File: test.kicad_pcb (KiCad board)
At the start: 4 copper layers, 112.7 x 43 mm, 85 parts, among them IC1 LC709203FQH-01TWG, IC2 BQ24074RGTR, IC3 USBLC6-2SC6, IC4 ESP32-S3-WROOM-1-N16, IC5 MCP6S91-E_MS, IC6 MCP6S91-E_MS, IC7 MCP4726A1T-E_CH, IC8 MCP4726A1T-E_CH, J1 UART0, J2 73100-0105, J3 73100-0105, K1 AQY210EHA, K2 AQY210EHA, SW1 Reset, SW2 Boot, U1 1043, U1 USB-C_SMD-TYPE-C-31-M-12, U2 1043, U4 LD1086DT33TR, U5 LD1086DT33TR, U6 LD1086DT33TR, U7 ADC08351CILQX/NOPB, U8 ADC08351CILQX/NOPB

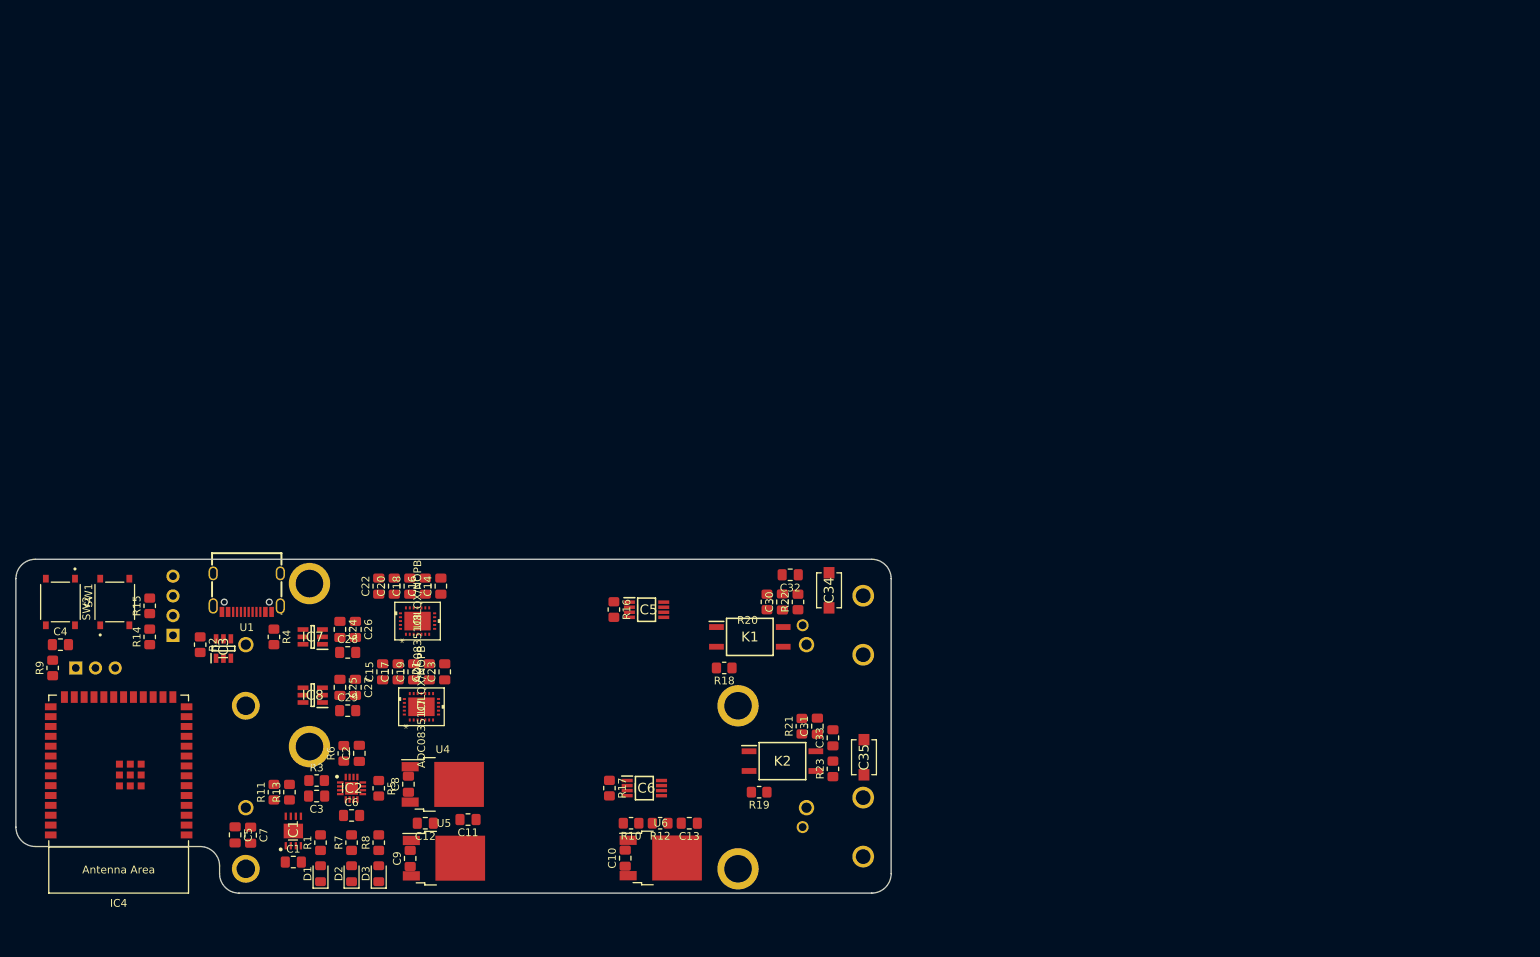
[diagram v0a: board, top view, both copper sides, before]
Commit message: layout for changed chematic
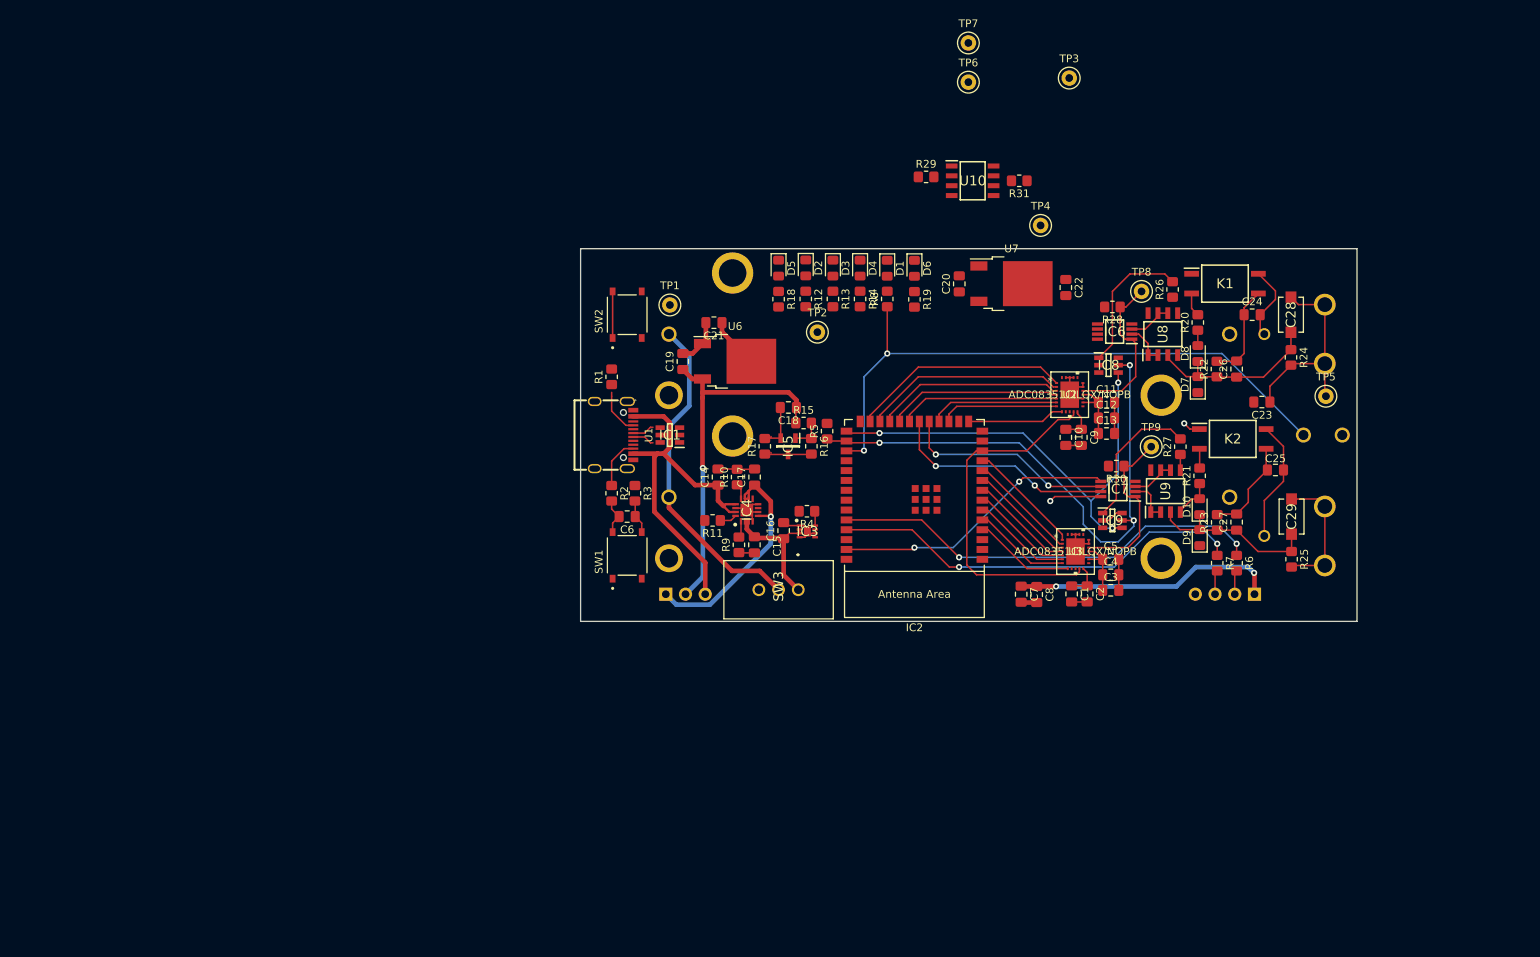
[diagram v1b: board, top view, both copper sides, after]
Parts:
- removed the C1 at (63.0, 129.0)
- removed the C10 at (105.8, 128.5)
- removed the C11 at (85.5, 123.5)
- removed the C12 at (80.0, 124.0)
- removed the C13 at (114.0, 124.0)
- removed the C2 at (71.5, 115.0)
- removed the C3 at (66.0, 120.5)
- removed C30, C31: 47n, Capacitor_SMD:C_0805_2012Metric_Pad1.18x1.45mm_HandSolder
- removed C32, C33: 100n, Capacitor_SMD:C_0805_2012Metric_Pad1.18x1.45mm_HandSolder
- removed C34, C35: 5.5p-30p var, project_library:JZ300
- removed the C6 at (70.5, 123.0)
- removed the C8 at (77.8, 119.0)
- removed the C9 at (78.0, 128.5)
- removed the IC1 at (63.0, 125.0)
- removed the IC2 at (70.5, 119.5)
- removed the J2 at (154.0, 124.5)
- removed the R2 at (51.0, 101.0)
- removed the R3 at (66.0, 118.5)
- removed the R6 at (69.5, 115.0)
- removed the R7 at (70.5, 126.5)
- removed the U1 at (56.9, 101.0)
- removed the U2 at (56.9, 122.0)
- added C14: 1u, Capacitor_SMD:C_0805_2012Metric_Pad1.18x1.45mm_HandSolder, F.Cu at (117.7, 79.4)
- added C15: 4u7, Capacitor_SMD:C_0805_2012Metric_Pad1.18x1.45mm_HandSolder, F.Cu at (122.4, 88.1)
- added C16: 0.1u, Capacitor_SMD:C_0805_2012Metric_Pad1.18x1.45mm_HandSolder, F.Cu at (126.2, 86.3)
- added C17: 4u7, Capacitor_SMD:C_0805_2012Metric_Pad1.18x1.45mm_HandSolder, F.Cu at (122.4, 79.4)
- added C18: 1u, Capacitor_SMD:C_0805_2012Metric_Pad1.18x1.45mm_HandSolder, F.Cu at (126.8, 70.5)
- added C19: 10u, Capacitor_SMD:C_0805_2012Metric_Pad1.18x1.45mm_HandSolder, F.Cu at (113.2, 64.5)
- added C20: 10u, Capacitor_SMD:C_0805_2012Metric_Pad1.18x1.45mm_HandSolder, F.Cu at (148.8, 54.5)
- added C21: 10u, Capacitor_SMD:C_0805_2012Metric_Pad1.18x1.45mm_HandSolder, F.Cu at (117.2, 59.5)
- added C22: 10u, Capacitor_SMD:C_0805_2012Metric_Pad1.18x1.45mm_HandSolder, F.Cu at (162.5, 55.0)
- added C23: 1u, Capacitor_SMD:C_0805_2012Metric_Pad1.18x1.45mm_HandSolder, F.Cu at (187.8, 69.8)
- added D10: ~, Diode_SMD:D_0805_2012Metric_Pad1.15x1.40mm_HandSolder, F.Cu at (179.7, 83.2)
- added D4: LOW_BATTERY, LED_SMD:LED_0805_2012Metric_Pad1.15x1.40mm_HandSolder, F.Cu at (136.0, 52.5)
- added D5: 3.3V, LED_SMD:LED_0805_2012Metric_Pad1.15x1.40mm_HandSolder, F.Cu at (125.5, 52.5)
- added D6: 3.3VA, LED_SMD:LED_0805_2012Metric_Pad1.15x1.40mm_HandSolder, F.Cu at (143.0, 52.5)
- added D7: ~, Diode_SMD:D_0805_2012Metric_Pad1.15x1.40mm_HandSolder, F.Cu at (179.5, 67.5)
- added D8: ~, Diode_SMD:D_0805_2012Metric_Pad1.15x1.40mm_HandSolder, F.Cu at (179.5, 63.5)
- added D9: ~, Diode_SMD:D_0805_2012Metric_Pad1.15x1.40mm_HandSolder, F.Cu at (179.8, 87.2)
- added IC3: MAX17048G+T10, project_library:MAX17048G+T10, F.Cu at (129.2, 86.4)
- added IC4: BQ24074RGTR, project_library:BQ24074RGTR, F.Cu at (121.4, 83.7)
- added IC9: DAC5571IDBVR, project_library:DAC5571IDBVR, F.Cu at (168.5, 85.0)
- added J1: PWM, project_library:725996-2, B.Cu at (199.0, 74.0)
- added J4: ~, project_library:73100-0105, B.Cu at (213.5, 87.0)
- added R14: 1k5, Resistor_SMD:R_0805_2012Metric_Pad1.20x1.40mm_HandSolder, F.Cu at (136.0, 56.5)
- added R15: 3k3, Resistor_SMD:R_0805_2012Metric_Pad1.20x1.40mm_HandSolder, F.Cu at (128.7, 72.5)
- added R24: ~, Resistor_SMD:R_0805_2012Metric_Pad1.20x1.40mm_HandSolder, F.Cu at (191.5, 64.0)
- added R25: ~, Resistor_SMD:R_0805_2012Metric_Pad1.20x1.40mm_HandSolder, F.Cu at (191.6, 90.0)
- added R26: ~, Resistor_SMD:R_0805_2012Metric_Pad1.20x1.40mm_HandSolder, F.Cu at (176.2, 55.2)
- added R27: ~, Resistor_SMD:R_0805_2012Metric_Pad1.20x1.40mm_HandSolder, F.Cu at (177.2, 75.5)
- added R28: ~, Resistor_SMD:R_0805_2012Metric_Pad1.20x1.40mm_HandSolder, F.Cu at (168.5, 57.5)
- added R29: ~, Resistor_SMD:R_0805_2012Metric_Pad1.20x1.40mm_HandSolder, F.Cu at (144.5, 40.8)
- added R30: ~, Resistor_SMD:R_0805_2012Metric_Pad1.20x1.40mm_HandSolder, F.Cu at (169.0, 78.0)
- added R31: ~, Resistor_SMD:R_0805_2012Metric_Pad1.20x1.40mm_HandSolder, F.Cu at (156.5, 41.2)
- added R4: 5k, Resistor_SMD:R_0805_2012Metric_Pad1.20x1.40mm_HandSolder, F.Cu at (129.2, 83.8)
- added R9: 10k, Resistor_SMD:R_0805_2012Metric_Pad1.20x1.40mm_HandSolder, F.Cu at (120.4, 88.1)
- added SW3: SW_DPDT_x2, project_library:25136NAH6, F.Cu at (125.5, 93.5)
- added TP1: VBat, TestPoint:TestPoint_Keystone_5000-5004_Miniature, F.Cu at (111.5, 57.2)
- added TP2: VBatChargeIC, TestPoint:TestPoint_Keystone_5000-5004_Miniature, F.Cu at (130.5, 60.8)
- added TP3: 3.3V, TestPoint:TestPoint_Keystone_5000-5004_Miniature, F.Cu at (162.9, 28.0)
- added TP4: 3.3VA, TestPoint:TestPoint_Keystone_5000-5004_Miniature, F.Cu at (159.2, 47.0)
- added TP5: GNDREF, TestPoint:TestPoint_Keystone_5000-5004_Miniature, F.Cu at (196.0, 69.0)
- added TP6: ~, TestPoint:TestPoint_Keystone_5000-5004_Miniature, F.Cu at (149.9, 28.6)
- added TP7: ~, TestPoint:TestPoint_Keystone_5000-5004_Miniature, F.Cu at (149.9, 23.5)
- added TP8: ~, TestPoint:TestPoint_Keystone_5000-5004_Miniature, F.Cu at (172.2, 55.5)
- added TP9: ~, TestPoint:TestPoint_Keystone_5000-5004_Miniature, F.Cu at (173.5, 75.5)
- added U10: ~, project_library:MCP6022T-I_SN, F.Cu at (150.5, 41.2)
- added U7: LD1086DT33TR, Package_TO_SOT_SMD:TO-252-2, F.Cu at (155.5, 54.5)
- added U8: ~, project_library:MCP6022T-I_SN, F.Cu at (175.0, 61.0)
- added U9: ~, project_library:MCP6022T-I_SN, F.Cu at (175.3, 81.2)
- C24, C25: value 0.1u -> ~
- C26, C27: value 10u -> ~
- C28, C29: value 0.1u -> ~; footprint Capacitor_SMD:C_0805_2012Metric_Pad1.18x1.45mm_HandSolder -> project_library:JZ300
- D1: value LOW_BATTERY -> Status
- IC5: value MCP6S91-E_MS -> LM4041CEM3-ADJ_NOPB; footprint project_library:MCP6S91-E_MS -> project_library:LM4041CEM3-ADJ_NOPB
- IC6: value MCP6S91-E_MS -> ~
- IC7: value MCP4726A1T-E_CH -> ~; footprint project_library:MCP4726A1T-E_CH -> project_library:MCP6S91-E_MS
- IC8: value MCP4726A1T-E_CH -> DAC5571IDBVR; footprint project_library:MCP4726A1T-E_CH -> project_library:DAC5571IDBVR
- J3: value 73100-0105 -> ~
- JP1: value Jumper_3_Open -> Power_Select
- K1, K2: value AQY210EHA -> ~
- R1: value 1k5 -> 5k1
- R10: value 39 -> 1k
- R11: value 5k -> 820
- R12: value 120 -> 1k5
- R13: value 5k -> 1k5
- R16: value 5k1 -> 1k
- R17: value 5k1 -> 330
- R18, R19: value 1k -> 1k5
- R20, R21: value 100k -> ~
- R22, R23: value 910k -> ~
- R5: value 1k -> 5k
- SW2: value Boot -> Button
- U4, U5: value LD1086DT33TR -> 1043; footprint Package_TO_SOT_SMD:TO-252-2 -> project_library:1043; moved to B.Cu
- moved R6 140.3 mm to (184.5, 90.5), turned to -90 degrees
- moved J2 139.4 mm to (186.8, 94.5), turned to 90 degrees
- moved R7 137.6 mm to (182.0, 90.5), turned to -90 degrees
- moved C28 129.1 mm to (191.5, 58.5), turned to 90 degrees
- moved C24 124.3 mm to (186.5, 58.5), turned to 0 degrees
- moved C29 124.1 mm to (191.6, 84.5), turned to 90 degrees
- moved C25 123.7 mm to (189.5, 78.5), turned to 0 degrees
- moved C26 118.4 mm to (184.5, 65.5), turned to 90 degrees
- moved C27 115.5 mm to (184.5, 85.2), turned to 90 degrees
- moved IC8 111.0 mm to (168.0, 65.0), turned to 0 degrees
- moved IC2 108.5 mm to (143.0, 81.8)
- moved D1 106.8 mm to (139.5, 52.5), turned to -90 degrees
- moved C7 105.9 mm to (156.8, 94.5)
- moved C8 105.9 mm to (158.8, 94.5)
- moved IC7 105.4 mm to (169.2, 81.0)
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- renumbered C14 to C1, C17 to C10, C19 to C11, C21 to C12, C23 to C13, C16 to C2, C18 to C3, C20 to C4, C22 to C5, C4 to C6, C5 to C7, C7 to C8, C15 to C9, IC3 to IC1, IC4 to IC2, J1 to J2, R4 to R2, R9 to R3, R14 to R6, R15 to R7, U7 to U2, U8 to U3
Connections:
- net /Charging renamed Charging
- net Net-(IC3-Pad4) renamed /D+
- net Net-(IC3-Pad6) renamed /D-
- C24 pad 2: GND -> Net-(C24-Pad2)
- C25 pad 2: GND -> Net-(C25-Pad2)
- C26 pad 1: Net-(C24-Pad1) -> Net-(C26-Pad1)
- C26 pad 2: GND -> Net-(C24-Pad1)
- C27 pad 1: Net-(C25-Pad1) -> Net-(C27-Pad1)
- C27 pad 2: GND -> Net-(C25-Pad1)
- C28 pad 1: Net-(C28-Pad1) -> Net-(C26-Pad1)
- C28 pad 2: GND -> GNDREF
- C29 pad 1: Net-(C29-Pad1) -> Net-(C27-Pad1)
- C29 pad 2: GND -> GNDREF
- IC2 pad 10: /CH1_D1 -> /CH2_D1
- IC2 pad 11: /CH1_D0 -> /CH2_D0
- IC2 pad 15: /CH2_D7 -> /CH1_D7
- IC2 pad 16: /LOG -> unconnected-(IC2-Pad16)
- IC2 pad 17: /CH2_D6 -> /CH1_D6
- IC2 pad 18: /CH2_D5 -> /CH1_D5
- IC2 pad 19: /MOSI -> MOSI
- IC2 pad 20: /SCLK -> SCLK_SPI
- IC2 pad 21: /CH2_D4 -> /CH1_D4
- IC2 pad 22: /CH2_D3 -> /CH1_D3
- IC2 pad 23: /CH2_D2 -> /CH1_D2
- IC2 pad 24: /CH2_D1 -> /CH1_D1
- IC2 pad 25: /CH2_D0 -> /CH1_D0
- IC2 pad 26: /VSPI -> unconnected-(IC2-Pad26)
- IC2 pad 27: /BOOT -> SDA
- IC2 pad 28: unconnected-(IC4-Pad28) -> SCL_I2C
- IC2 pad 29: unconnected-(IC4-Pad29) -> /Status_PWM
- IC2 pad 30: unconnected-(IC4-Pad30) -> Trigger_Ref
- IC2 pad 31: /CH1_Gnd_Sel -> Trigger_CH1
- IC2 pad 32: /CH2_Gnd_Sel -> Trigger_CH2
- IC2 pad 33: /CS_A -> CH1_AC_Sel
- IC2 pad 34: /CS_B -> CH2_AC_Sel
- IC2 pad 38: /SCL -> CS_Gain_CH1
- IC2 pad 39: /SDA -> CS_Gain_CH2
- IC2 pad 4: /CH1_D7 -> /CH2_D7
- IC2 pad 5: /CH1_D6 -> /CH2_D6
- IC2 pad 6: /CH1_D5 -> /CH2_D5
- IC2 pad 7: /CH1_D4 -> /CH2_D4
- IC2 pad 8: /CH1_D3 -> /CH2_D3
- IC2 pad 9: /CH1_D2 -> /CH2_D2
- IC5 pad 1: Net-(IC5-Pad1) -> GNDREF
- IC5 pad 2: unconnected-(IC5-Pad2) -> GNDA
- IC5 pad 3: GND -> Net-(IC5-Pad3)
- IC6 pad 1: Net-(IC6-Pad1) -> Analog_Out_CH1
- IC6 pad 2: unconnected-(IC6-Pad2) -> Net-(IC6-Pad2)
- IC6 pad 3: GND -> Net-(IC6-Pad3)
- IC6 pad 5: /CS_A -> CS_Gain_CH1
- IC6 pad 6: /MOSI -> MOSI
- IC6 pad 7: /SCLK -> SCLK_SPI
- IC6 pad 8: +3V3 -> +3.3VA
- IC7 pad 1: Net-(C28-Pad1) -> Analog_Out_CH2
- IC7 pad 2: GND -> Net-(IC7-Pad2)
- IC7 pad 3: Net-(C24-Pad1) -> Net-(IC7-Pad3)
- IC7 pad 4: /SDA -> GND
- IC7 pad 5: /SCL -> CS_Gain_CH2
- IC7 pad 6: unconnected-(IC7-Pad6) -> MOSI
- IC8 pad 1: Net-(C29-Pad1) -> /Analog/Offset_CH1
- IC8 pad 3: Net-(C25-Pad1) -> +3.3VA
- IC8 pad 4: /SDA -> SDA
- IC8 pad 5: /SCL -> SCL_I2C
- IC8 pad 6: unconnected-(IC8-Pad6) -> +3V3
- J3 pad 1: GND -> GNDREF
- J3 pad 2: GND -> GNDREF
- J3 pad 3: Net-(C35-Pad1) -> Net-(C24-Pad2)
- JP1 pad 1: /Vbat -> Net-(C17-Pad1)
- JP1 pad 2: Net-(C10-Pad1) -> Net-(C18-Pad1)
- K1 pad 1: /CH1_Gnd_Sel -> CH1_AC_Sel
- K1 pad 3: Net-(C32-Pad1) -> Net-(C24-Pad1)
- K1 pad 4: Net-(C30-Pad1) -> Net-(C24-Pad2)
- K2 pad 1: /CH2_Gnd_Sel -> CH2_AC_Sel
- K2 pad 3: Net-(C33-Pad1) -> Net-(C25-Pad1)
- K2 pad 4: Net-(C31-Pad1) -> Net-(C25-Pad2)
- R1 pad 1: Net-(D1-Pad2) -> Net-(R1-Pad1)
- R1 pad 2: /Alarm -> GND
- R10 pad 1: Net-(R10-Pad1) -> Net-(IC4-Pad12)
- R11 pad 1: /SCL -> Net-(IC4-Pad16)
- R11 pad 2: +3V3 -> GND
- R12 pad 1: GND -> Net-(D2-Pad2)
- R12 pad 2: Net-(R10-Pad1) -> Net-(C17-Pad1)
- R13 pad 1: /SDA -> Net-(D3-Pad2)
- R13 pad 2: +3V3 -> Net-(C17-Pad1)
- R16 pad 1: Net-(IC5-Pad1) -> GNDREF
- R16 pad 2: GND -> Net-(IC5-Pad3)
- R17 pad 1: Net-(IC6-Pad1) -> Net-(IC5-Pad3)
- R17 pad 2: GND -> GNDA
- R18 pad 1: GND -> Net-(D5-Pad2)
- R18 pad 2: Net-(K1-Pad2) -> +3V3
- R19 pad 1: GND -> Net-(D6-Pad2)
- R19 pad 2: Net-(K2-Pad2) -> +3.3VA
- R2 pad 1: Net-(R4-Pad1) -> Net-(R2-Pad1)
- R20 pad 1: Net-(C30-Pad1) -> GNDA
- R20 pad 2: GND -> Net-(K1-Pad2)
- R21 pad 1: Net-(C31-Pad1) -> GNDA
- R21 pad 2: GND -> Net-(K2-Pad2)
- R22 pad 1: Net-(C34-Pad1) -> Net-(C26-Pad1)
- R22 pad 2: Net-(C32-Pad1) -> Net-(C24-Pad1)
- R23 pad 1: Net-(C35-Pad1) -> Net-(C27-Pad1)
- R23 pad 2: Net-(C33-Pad1) -> Net-(C25-Pad1)
- R5 pad 1: Net-(IC2-Pad12) -> SCL_I2C
- R5 pad 2: GND -> +3V3
- R8 pad 1: Net-(D3-Pad2) -> /Status_PWM
- R8 pad 2: /Vbat -> Net-(D1-Pad2)
- SW1 pad A: GND -> unconnected-(SW1-PadA)
- SW1 pad C: /ENABLE -> unconnected-(SW1-PadC)
- SW2 pad A: /BOOT -> SDA
- SW2 pad B: /BOOT -> SDA
- U2 pad 10: +3V3 -> unconnected-(U2-Pad10)
- U2 pad 14: unconnected-(U7-Pad14) -> +3.3VA
- U2 pad 17: unconnected-(U7-Pad17) -> Analog_Out_CH1
- U2 pad 25: (no net) -> GND
- U3 pad 10: +3V3 -> unconnected-(U3-Pad10)
- U3 pad 17: unconnected-(U8-Pad17) -> Analog_Out_CH2
- U3 pad 25: (no net) -> GND
- U4 pad 1: GND -> /Power Supply/VBat+
- U4 pad 2: +3V3 -> GND
- U5 pad 1: GND -> /Power Supply/VBat+
- U5 pad 2: +3.3VA -> GND
- U6 pad 1: Net-(R10-Pad1) -> GND
- U6 pad 2: GND -> +3V3
- U6 pad 3: Net-(C10-Pad1) -> Net-(C18-Pad1)
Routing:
- net /Status_PWM: track 0.00 -> 80.0 mm, vias 0 -> 2
- net GND: track 0.00 -> 71.8 mm
- net SCL_I2C: track 0.00 -> 71.1 mm, vias 0 -> 3
- net SDA: track 0.00 -> 67.7 mm, vias 0 -> 3
- net /RX0: track 0.00 -> 56.3 mm, vias 0 -> 2
- net /TX0: track 0.00 -> 53.7 mm, vias 0 -> 2
- net +3V3: track 0.00 -> 50.8 mm, vias 0 -> 2
- net +5V: track 0.00 -> 50.8 mm
- net GNDREF: track 0.00 -> 48.7 mm
- net Net-(C18-Pad1): track 0.00 -> 47.5 mm, vias 0 -> 1
- net /I2S_CLK: track 0.00 -> 45.7 mm
- net /Power Supply/VBat+: track 0.00 -> 43.0 mm
- net CS_Gain_CH2: track 0.00 -> 36.8 mm, vias 0 -> 2
- net Net-(C17-Pad1): track 0.00 -> 31.2 mm, vias 0 -> 1
- net SCLK_SPI: track 0.00 -> 29.2 mm, vias 0 -> 2
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- added copper zone on In1.Cu, net GND
- added copper zone on In2.Cu, net GND
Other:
- board size 112.7 x 43 mm -> 100 x 48 mm

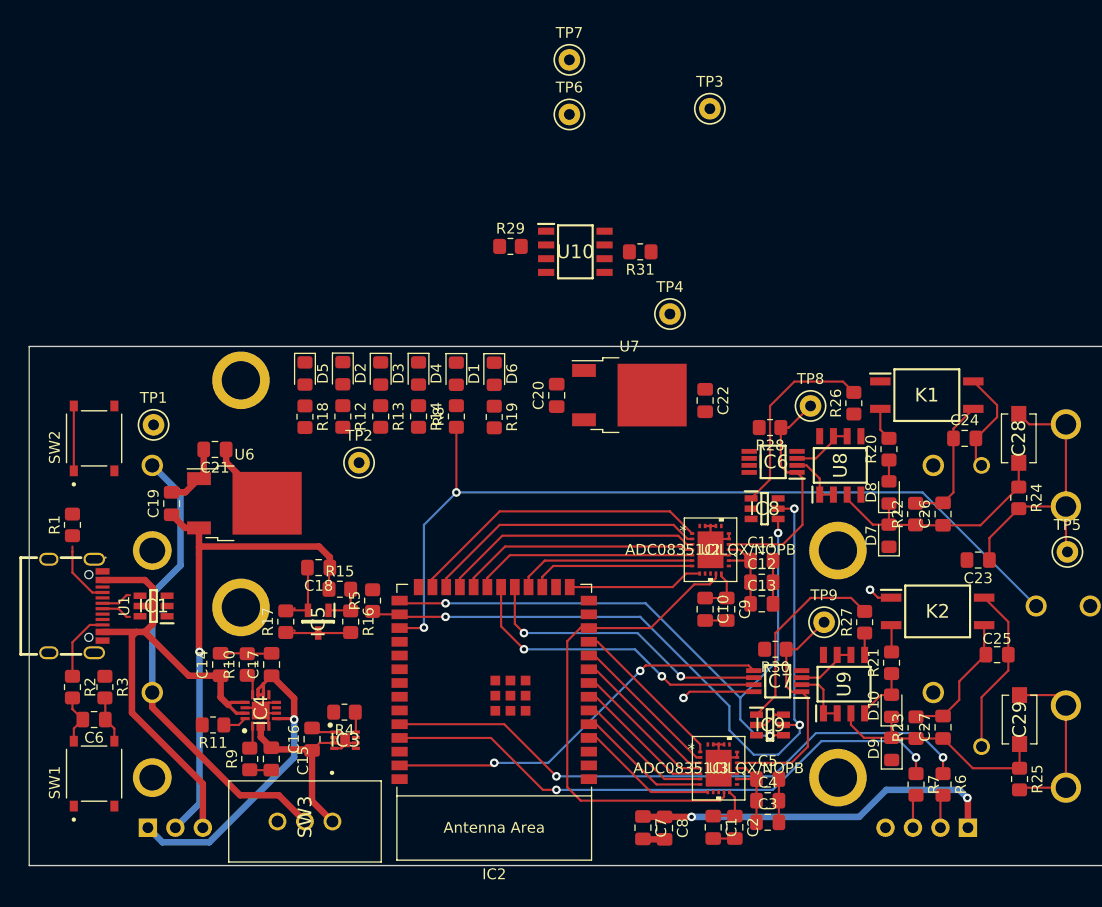
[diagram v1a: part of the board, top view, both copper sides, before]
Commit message: small fix for jlcpcb parts detection
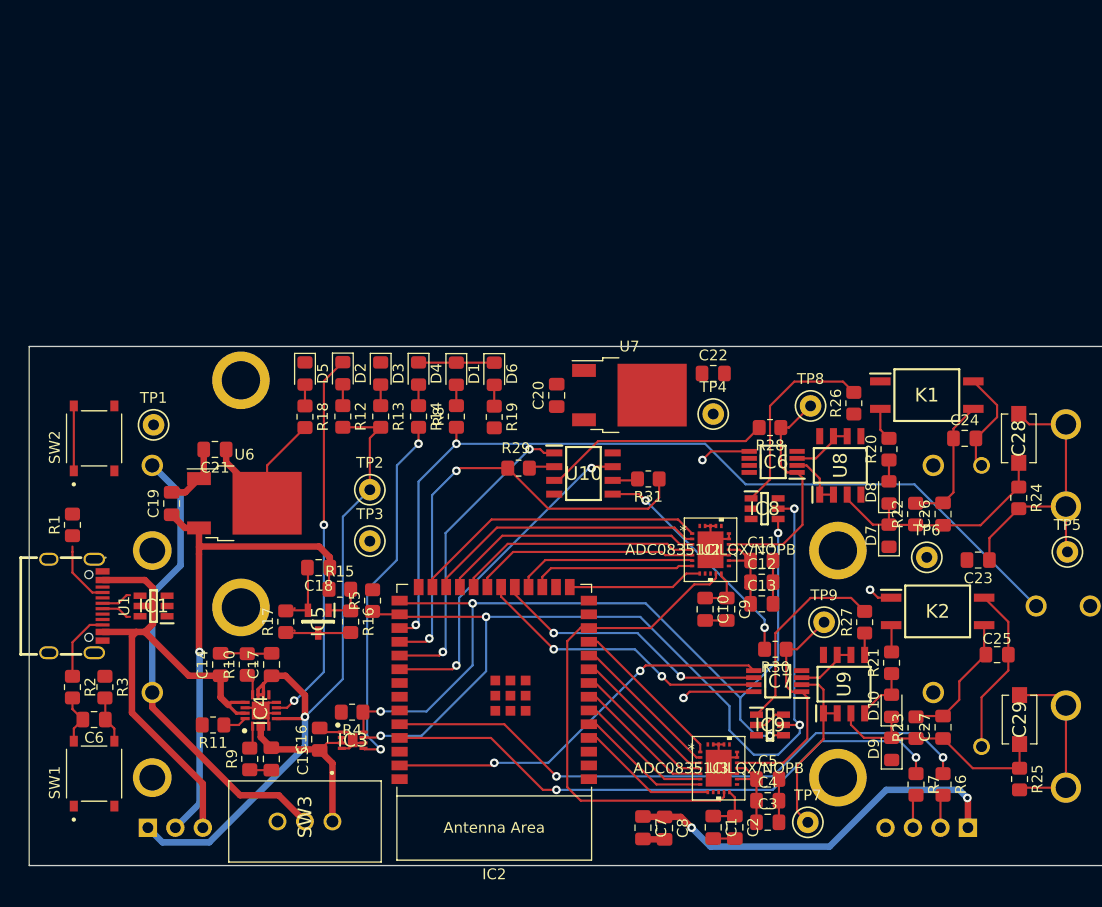
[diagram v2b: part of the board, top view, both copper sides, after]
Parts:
- R4, R5: value 5k -> 6k8
- moved TP7 73.9 mm to (172.0, 94.0)
- moved TP6 52.6 mm to (183.0, 69.5)
- moved TP3 50.9 mm to (131.5, 68.0)
- moved R31 21.0 mm to (157.2, 62.2)
- moved R29 20.5 mm to (145.2, 61.2)
- moved U10 20.5 mm to (151.2, 61.8)
- moved TP4 10.1 mm to (163.2, 56.2)
- moved TP2 2.69 mm to (131.5, 63.2)
- moved C22 2.61 mm to (163.2, 52.5), turned to 0 degrees
- moved C16 0.70 mm to (126.9, 86.3)
- moved IC3 0.70 mm to (129.9, 86.4)
- moved R4 0.70 mm to (129.9, 83.8)
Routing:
- net Trigger_Ref: track 0.00 -> 42.0 mm, vias 0 -> 2
- net Net-(C17-Pad1): track 31.2 -> 67.0 mm
- net Net-(D2-Pad1): track 0.00 -> 35.1 mm, vias 0 -> 2
- net /Power Supply/Alarm: track 0.00 -> 33.9 mm, vias 0 -> 2
- net Trigger_CH2: track 0.00 -> 31.0 mm, vias 0 -> 2
- net Trigger_CH1: track 0.00 -> 28.6 mm, vias 0 -> 2
- net Net-(R30-Pad2): track 0.00 -> 21.6 mm, vias 0 -> 2
- net Net-(R28-Pad2): track 0.00 -> 21.0 mm
- net SCL_I2C: track 71.1 -> 90.0 mm, vias 3 -> 4
- net SDA: track 67.7 -> 85.6 mm, vias 3 -> 4
- net Net-(IC7-Pad2): track 5.67 -> 17.2 mm
- net +3V3: track 50.8 -> 60.4 mm
- net GNDA: track 6.04 -> 11.5 mm
- net CS_Gain_CH1: track 0.00 -> 4.66 mm, vias 0 -> 1
- net Net-(R31-Pad2): track 0.00 -> 2.36 mm
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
